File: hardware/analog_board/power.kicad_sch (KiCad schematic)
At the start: 0 parts

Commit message: feat：模拟板电源 原理图设计
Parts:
- added C121, C122, C131, C135, C136, C142, C147, C149, C153, C158, C159, C162, C163, C169, C171, C173, C174, C177: 100nF, Capacitor_SMD:C_0603_1608Metric, symbol Device:C
- added C123: 330pF, Capacitor_SMD:C_0603_1608Metric, symbol Device:C
- added C124, C148: 33nF, Capacitor_SMD:C_0603_1608Metric, symbol Device:C
- added C125, C126, C129, C130, C133, C134, C143, C145, C146, C166: 1uF, Capacitor_SMD:C_0603_1608Metric, symbol Device:C
- added C127, C128, C132, C139, C144, C150, C151, C152, C156, C157, C160, C161, C164, C165, C167, C168, C170, C172: 100uF, Capacitor_SMD:C_Elec_6.3x7.7, symbol Device:C_Polarized
- added C137: 1.2nF, Capacitor_SMD:C_0603_1608Metric, symbol Device:C
- added C138: 2.2uF, Capacitor_SMD:C_0603_1608Metric, symbol Device:C
- added C140, C141, C154, C155: 22uF, Capacitor_SMD:C_1206_3216Metric, symbol Device:C
- added C175, C176: 10uF, Capacitor_SMD:C_0603_1608Metric, symbol Device:C
- added D2, D3, D4: SS34, Diode_SMD:D_SMA, symbol Diode:SS34
- added HS1, HS2, HS3, HS4: Heatsink_Pad, Heatsink:TO-220_Heatsink, symbol Mechanical:Heatsink_Pad
- added L13: 33uH, Inductor_SMD:L_Changjiang_FXL1040, symbol Device:L
- added L14: 150uH, Inductor_SMD:L_12x12mm_H6mm, symbol Device:L
- added L15: 2.2uH, Inductor_SMD:L_Changjiang_FXL0420, symbol Device:L
- added R61: 1.6kR, Resistor_SMD:R_0603_1608Metric, symbol Device:R
- added R62: 196kR, Resistor_SMD:R_0603_1608Metric, symbol Device:R
- added R63: 77.5k, Resistor_SMD:R_0603_1608Metric, symbol Device:R
- added R64, R68, R71: 10kR, Resistor_SMD:R_0603_1608Metric, symbol Device:R
- added R65: 237kR, Resistor_SMD:R_0603_1608Metric, symbol Device:R
- added R66: 3.3kR, Resistor_SMD:R_0603_1608Metric, symbol Device:R
- added R67: 77.5kR, Resistor_SMD:R_0603_1608Metric, symbol Device:R
- added R69: 15k, Resistor_SMD:R_0603_1608Metric, symbol Device:R
- added R70: 2.4kR, Resistor_SMD:R_0603_1608Metric, symbol Device:R
- added R72: 12kR, Resistor_SMD:R_0603_1608Metric, symbol Device:R
- added R73: 68kR, Resistor_SMD:R_0603_1608Metric, symbol Device:R
- added R74: 7.5kR, Resistor_SMD:R_0603_1608Metric, symbol Device:R
- added U10, U9: TPS54360DDA, Package_SO:TI_SO-PowerPAD-8_ThermalVias, symbol Regulator_Switching:TPS54360DDA
- added U11: TPS62933, Package_TO_SOT_SMD:SOT-583-8, symbol Regulator_Switching:TPS62933
- added U12: L7805, Package_TO_SOT_THT:TO-220-3_Vertical, symbol Regulator_Linear:L7805
- added U13: L7905, Package_TO_SOT_THT:TO-220-3_Vertical, symbol Regulator_Linear:L7905
- added U14: TPS7A4701xRGW, Package_DFN_QFN:Texas_RGW0020A_VQFN-20-1EP_5x5mm_P0.65mm_EP3.15x3.15mm_ThermalVias, symbol Regulator_Linear:TPS7A4701xRGW
- added U15: TPS7A91, Package_DFN_QFN:Texas_S-PDSO-N10_EP1.2x2mm, symbol Regulator_Linear:TPS7A91
- added U16: L7815, Package_TO_SOT_THT:TO-220-3_Vertical, symbol Regulator_Linear:L7815
- added U17: L7915, Package_TO_SOT_THT:TO-220-3_Vertical, symbol Regulator_Linear:L7915
- added U19: AMS1117, Package_TO_SOT_SMD:SOT-223-3_TabPin2, symbol Regulator_Linear:AMS1117
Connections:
- new net: R73.1, R74.2, U19.1 (ADJ)
- new net: C148.1, U11.7 (SS)
- new net: R62.2, U9.4 (RT/CLK)
- new net: C138.1, R66.1
- new net: C122.2, U9.1 (BOOT)
- new net: C123.1, R61.2, U9.6 (COMP)
- new net: C122.1, D3.1 (K), L13.1, U9.8 (SW)
- new net: C171.2, U15.8 (NR/SS)
- new net: C124.1, R61.1
- new net: R69.1, R72.2, U15.3 (FB)
- new net: C149.1, D4.1 (K), L15.1, U11.5 (SW)
- new net: C166.2, U14.14 (NR)
- new net: C137.1, R66.2, U10.6 (COMP)
- new net: C149.2, U11.6 (BST)
- new net: C136.2, U10.1 (BOOT)
- new net: R65.2, U10.4 (RT/CLK)
- new net: C136.1, D2.1 (K), L14.1, U10.8 (SW)
- new net +1.8VA: C172.1, C173.2, R69.2, U15.1 (OUT), U15.2 (OUT)
- new net +1.8VD: C176.2, C177.2, R73.2, U19.2 (VO)
- new net +15VA: C156.1, C158.2, U16.3 (OUT)
- new net +17V: C121.2, C125.2, C126.2, C127.1, C132.1, C133.2, C134.2, C135.2, C143.2, C144.1, C145.2, C146.2, C147.2, C150.1, U10.2 (VIN), U11.3 (VIN), U16.1 (IN), U9.2 (VIN)
- new net +3.3V: C174.2, C175.2, U19.3 (VI)
- new net +3.3VA: C168.1, C169.2, C170.1, U14.1 (OUT), U14.2 (NC), U14.20 (OUT), U14.3 (SENSE/FB), U15.10 (IN), U15.6 (SS_CTRL), U15.7 (EN), U15.9 (IN)
- new net +5VA: C160.1, C162.2, C167.1, U12.3 (OUT), U14.13 (EN), U14.15 (IN), U14.16 (IN)
- new net +7V: C128.1, C129.2, C130.2, C131.2, C164.1, L13.2, R63.2, U12.1 (IN)
- new net -15VA: C157.2, C159.1, U17.3 (VO)
- new net -17V: C151.2, U17.2 (VI)
- new net -5VA: C161.2, C163.1, U13.3 (VO)
- new net -7V: C137.2, C138.2, C139.2, C140.1, C141.1, C142.1, C143.1, C152.2, C153.1, C154.1, C155.1, C165.2, D2.2 (A), D4.2 (A), R65.1, R68.1, R71.1, U10.7 (GND), U10.9 (GNDPAD), U13.2 (VI)
- new net FB+: R63.1, R64.2, U9.5 (FB)
- new net FB-: R67.1, R68.2, U10.5 (FB)
- new net FB_1.0V: R70.1, R71.2, U11.8 (FB)
- new net GND: C121.1, C123.2, C124.2, C125.1, C126.1, C127.2, C128.2, C129.1, C130.1, C131.1, C132.2, C133.1, C134.1, C135.1, C139.1, C140.2, C141.2, C142.2, C144.2, C145.1, C146.1, C147.1, C148.2, C150.2, C151.1, C152.1, C153.2, C154.2, C155.2, C156.2, C157.1, C158.1, C159.2, C160.2, C161.1, C162.1, C163.2, C164.2, C165.1, C166.1, C167.2, C168.2, C169.1, C170.2, C171.1, C172.2, C173.1, C174.1, C175.1, C176.1, C177.1, D3.2 (A), HS1.1, HS2.1, HS3.1, HS4.1, L14.2, L15.2, R62.1, R64.1, R67.2, R70.2, R72.1, R74.1, U11.4 (GND), U12.2 (GND), U13.1 (GND), U14.11 (0.2V), U14.12 (0.1V), U14.17 (NC), U14.18 (NC), U14.19 (NC), U14.21 (EP), U14.7 (GND), U14.8 (1.6V), U15.11 (GND), U15.4 (GND), U16.2 (GND), U17.1 (GND), U9.7 (GND), U9.9 (GNDPAD)

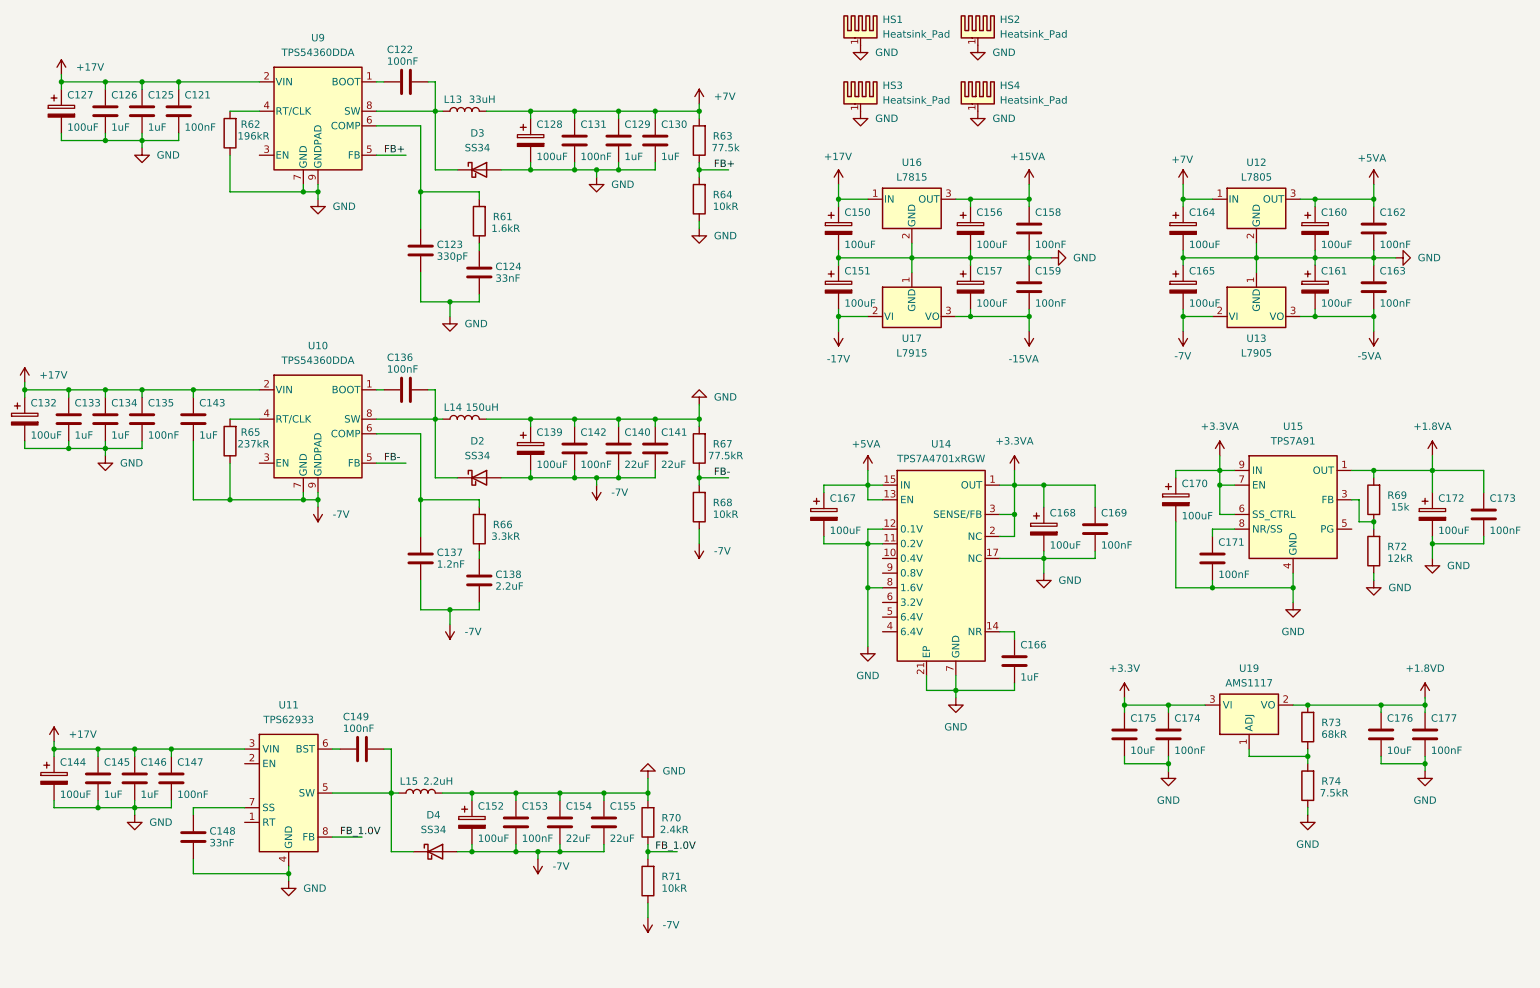
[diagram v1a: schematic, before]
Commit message: fixbug：修复 1.0V DCDC错误；根据PCB布局修改DCDC输入/输出电解电容参数
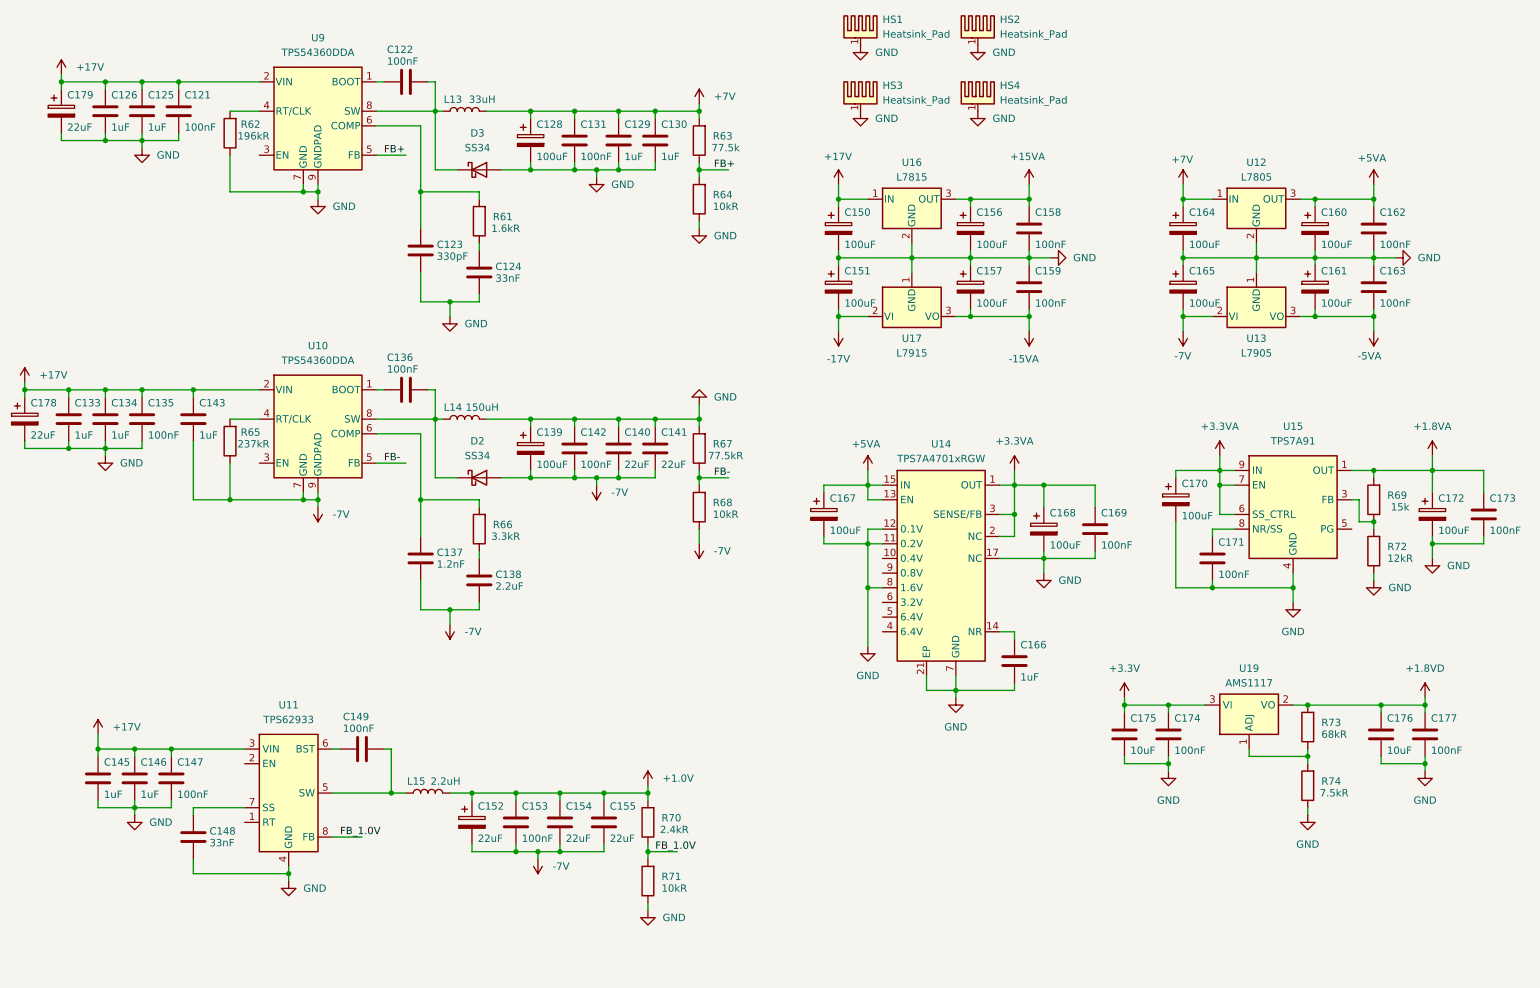
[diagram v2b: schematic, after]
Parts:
- removed C127, C132, C144: 100uF, Capacitor_SMD:C_Elec_6.3x7.7, symbol Device:C_Polarized
- removed D4: SS34, Diode_SMD:D_SMA, symbol Diode:SS34
- added C178, C179: 22uF, Capacitor_SMD:CP_Elec_5x5.4, symbol Device:C_Polarized
- C152: value 100uF -> 22uF; footprint Capacitor_SMD:C_Elec_6.3x7.7 -> Capacitor_SMD:CP_Elec_5x5.4
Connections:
- net +17V: now also C178.1, C179.1
- net -7V: no longer R71.1
- net GND: now also R71.1, C178.2, C179.2; no longer C152.1, C153.2, C154.2, C155.2, L15.2, R70.2
- new net +1.0V: C152.1, C153.2, C154.2, C155.2, L15.2, R70.2
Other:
- moved on the sheet: L15

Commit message: feat：原理图添加测试点
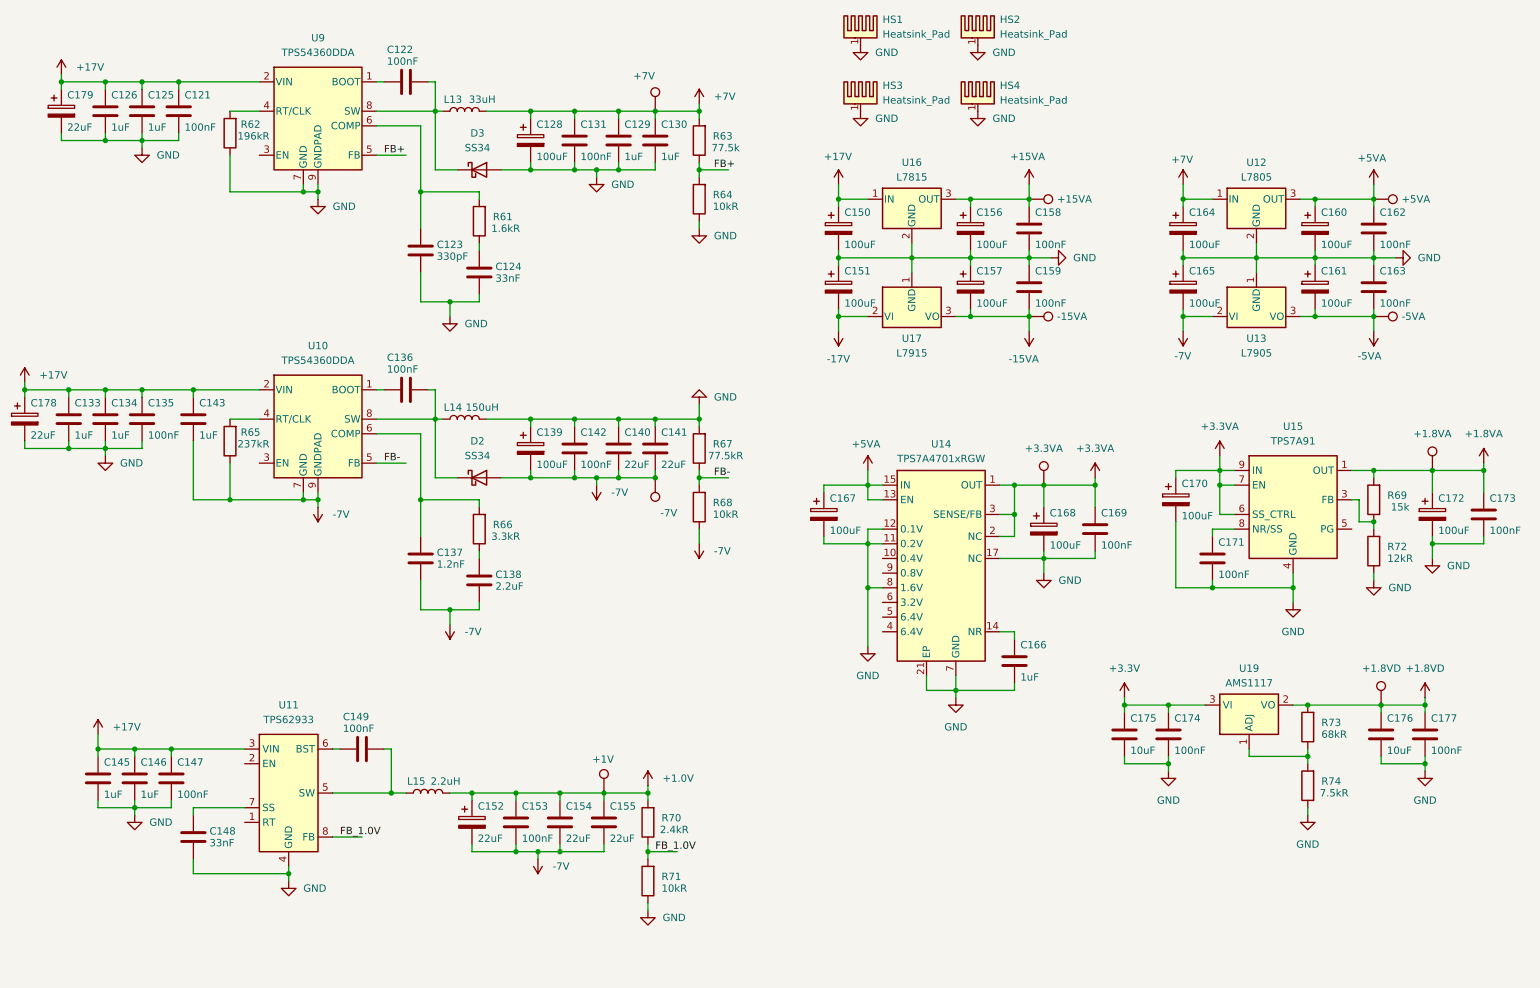
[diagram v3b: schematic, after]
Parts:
- added TP10: -7V, TestPoint:TestPoint_Pad_D1.0mm, symbol Connector:TestPoint
- added TP11: +1V, TestPoint:TestPoint_Pad_D1.0mm, symbol Connector:TestPoint
- added TP12: +15VA, TestPoint:TestPoint_Pad_D1.0mm, symbol Connector:TestPoint
- added TP13: -15VA, TestPoint:TestPoint_Pad_D1.0mm, symbol Connector:TestPoint
- added TP14: -5VA, TestPoint:TestPoint_Pad_D1.0mm, symbol Connector:TestPoint
- added TP15: +5VA, TestPoint:TestPoint_Pad_D1.0mm, symbol Connector:TestPoint
- added TP16: +3.3VA, TestPoint:TestPoint_Pad_D1.0mm, symbol Connector:TestPoint
- added TP17: +1.8VA, TestPoint:TestPoint_Pad_D1.0mm, symbol Connector:TestPoint
- added TP18: +1.8VD, TestPoint:TestPoint_Pad_D1.0mm, symbol Connector:TestPoint
- added TP9: +7V, TestPoint:TestPoint_Pad_D1.0mm, symbol Connector:TestPoint
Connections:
- net +1.0V: now also TP11.1
- net +1.8VA: now also TP17.1
- net +1.8VD: now also TP18.1
- net +15VA: now also TP12.1
- net +3.3VA: now also TP16.1
- net +5VA: now also TP15.1
- net +7V: now also TP9.1
- net -15VA: now also TP13.1
- net -5VA: now also TP14.1
- net -7V: now also TP10.1

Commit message: feat：根据PCB微调原理图
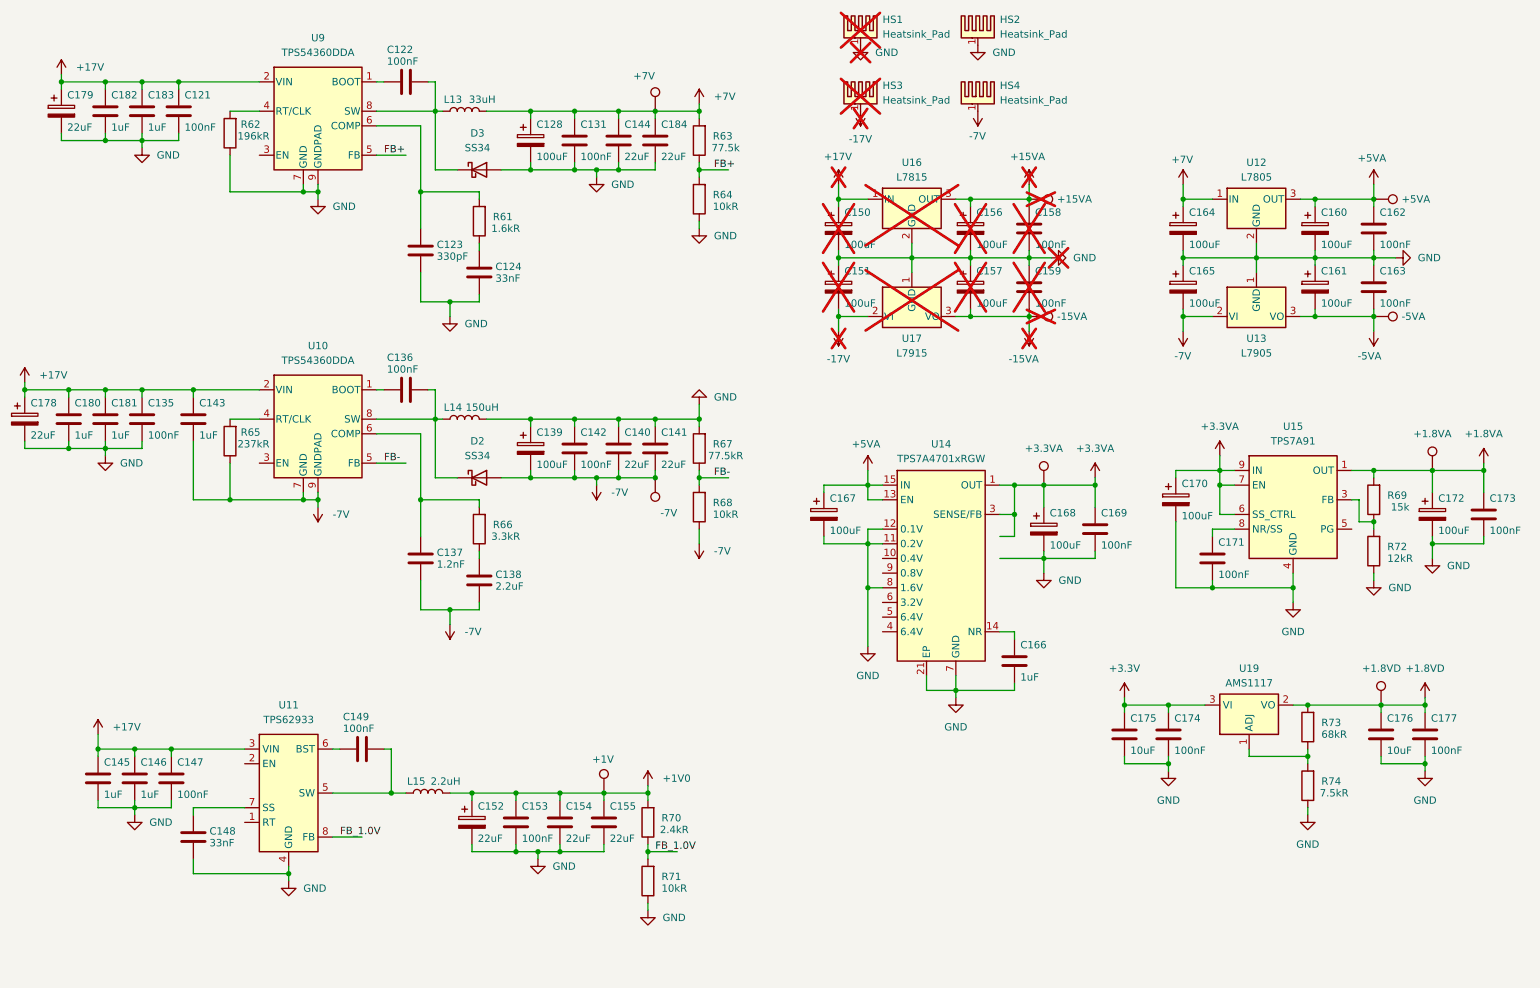
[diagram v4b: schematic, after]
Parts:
- removed C125, C126, C129, C130, C133, C134: 1uF, Capacitor_SMD:C_0603_1608Metric, symbol Device:C
- added C144, C184: 22uF, Capacitor_SMD:C_1206_3216Metric, symbol Device:C
- added C180, C181, C182, C183: 1uF, Capacitor_SMD:C_1206_3216Metric, symbol Device:C
- C145, C146: footprint Capacitor_SMD:C_0603_1608Metric -> Capacitor_SMD:C_1206_3216Metric
- C150, C151, C156, C157, C158, C159, HS1, HS3, TP12, TP13, U16, U17: now not fitted
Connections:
- net +17V: now also C180.2, C181.2, C182.2, C183.2
- net +3.3VA: no longer U14.2 (NC)
- net +7V: now also C144.2, C184.2
- net -17V: now also HS3.1
- net -7V: now also HS4.1; no longer C152.2, C153.1, C154.1, C155.1
- net GND: now also C152.2, C153.1, C154.1, C155.1, C144.1, C180.1, C181.1, C182.1, C183.1, C184.1; no longer HS3.1, HS4.1, U14.17 (NC), U14.18 (NC), U14.19 (NC)
- net +1.0V renamed +1V0

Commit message: feat：添加缝合过孔
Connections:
- net +3.3VA: now also U14.2 (NC)
- net GND: now also U14.17 (NC), U14.18 (NC), U14.19 (NC)
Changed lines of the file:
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@@
 		(pin "21"
+		)
+		(pin "2"
+		)
+		(pin "19"
+		)
+		(pin "17"
+		)
+		(pin "18"
 		)
 		(instances
